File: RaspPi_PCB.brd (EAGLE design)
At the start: 105.4 x 83.8 mm, 5 parts, among them J3 1X2-3.5MM

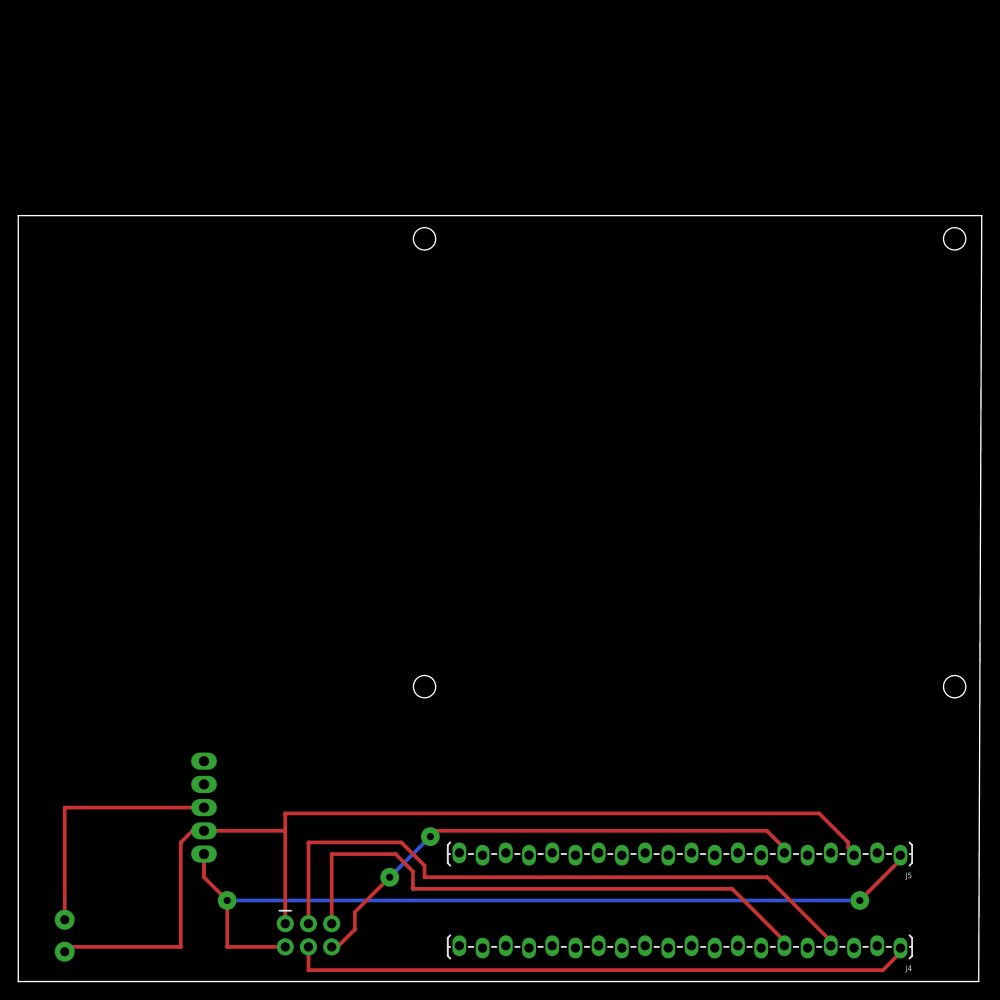
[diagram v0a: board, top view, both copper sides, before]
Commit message: Change RaspPi board to switch the side that the Pi is on and to switch the two Pi headers.
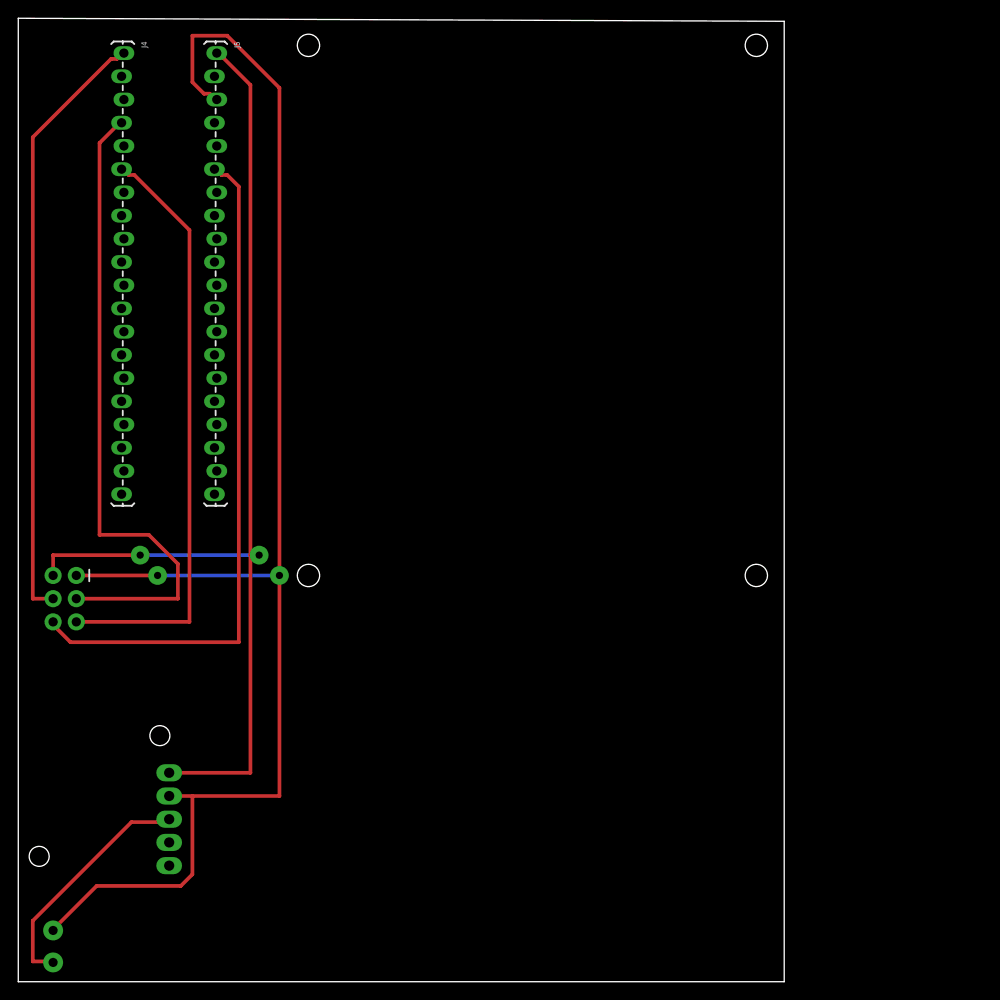
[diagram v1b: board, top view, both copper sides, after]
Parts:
- moved J4 129.6 mm to (11.4, 101.6), turned to 270 degrees
- moved J5 115.3 mm to (21.6, 101.6), turned to 270 degrees
- moved J1 45.5 mm to (5.08, 41.9), turned to 0 degrees
- moved J2 9.67 mm to (16.5, 22.9), turned to 270 degrees
- moved J3 1.80 mm to (3.81, 3.81), turned to 90 degrees
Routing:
- net GND: track 113.3 -> 158.6 mm, vias 0 -> 2
- net 5V: track 93.6 -> 115.0 mm
- net PIN18: track 57.6 -> 74.7 mm, vias 2 -> 0
- net PIN17: track 62.7 -> 65.4 mm
- net 3.3V: track 68.6 -> 66.5 mm
- net VIN: track 27.5 -> 26.3 mm
- net PIN4: track 71.8 -> 71.0 mm
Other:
- board size 105.4 x 83.8 mm -> 83.8 x 105.4 mm

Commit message: Rotate main pcb so it can be printed on the other mill.
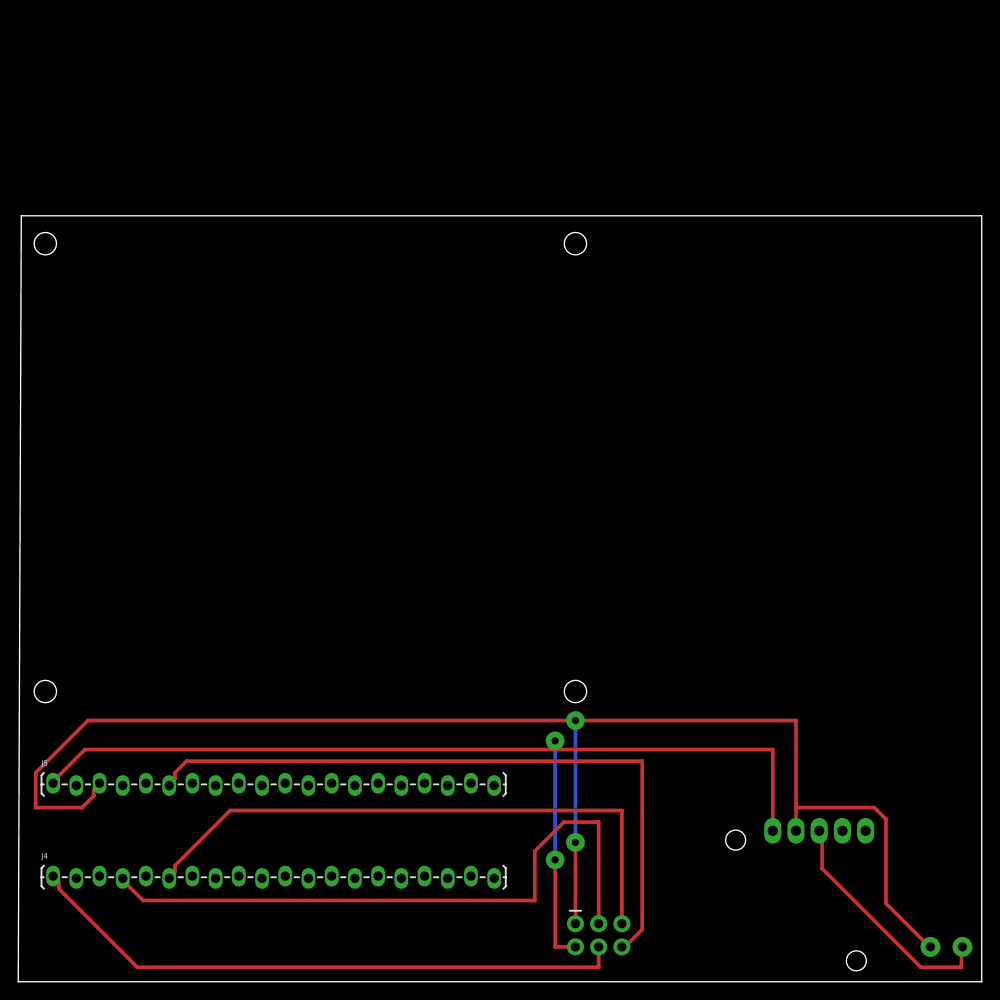
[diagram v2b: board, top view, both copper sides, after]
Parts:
- moved J3 97.8 mm to (101.6, 3.81), turned to 0 degrees
- moved J4 90.5 mm to (3.81, 11.4), turned to 0 degrees
- moved J5 82.0 mm to (3.81, 21.6), turned to 0 degrees
- moved J1 69.1 mm to (63.5, 5.08), turned to 270 degrees
- moved J2 66.3 mm to (82.5, 16.5), turned to 180 degrees
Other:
- board size 83.8 x 105.4 mm -> 105.4 x 83.8 mm

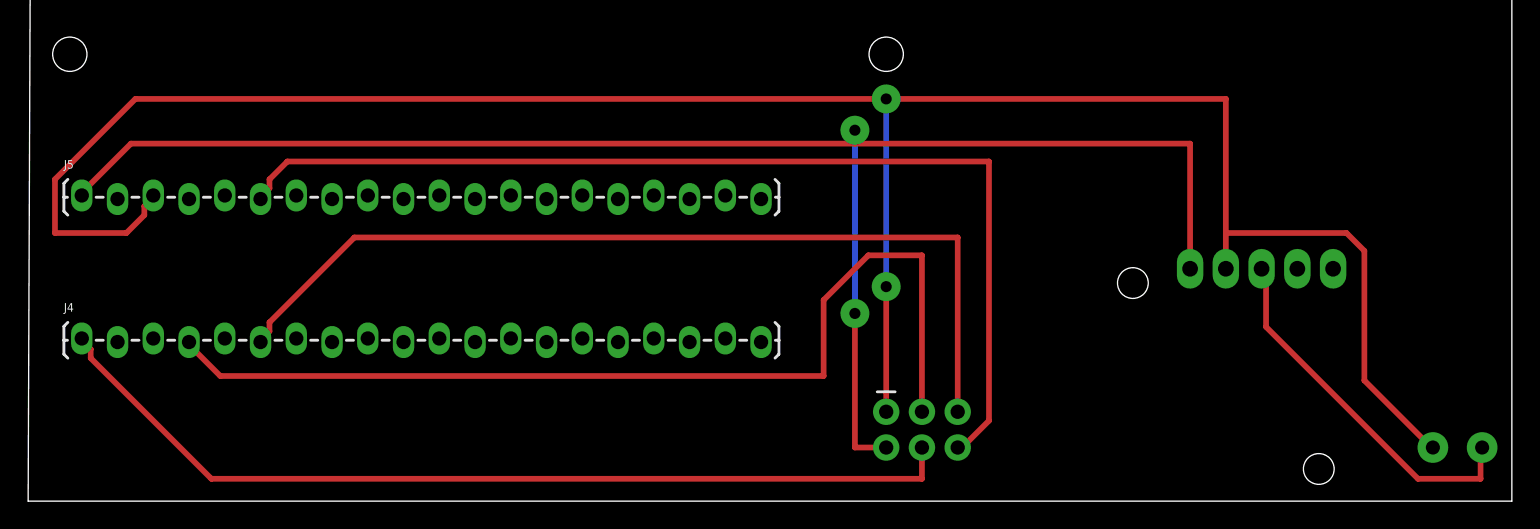
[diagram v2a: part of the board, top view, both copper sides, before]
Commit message: Flip voltage regulator
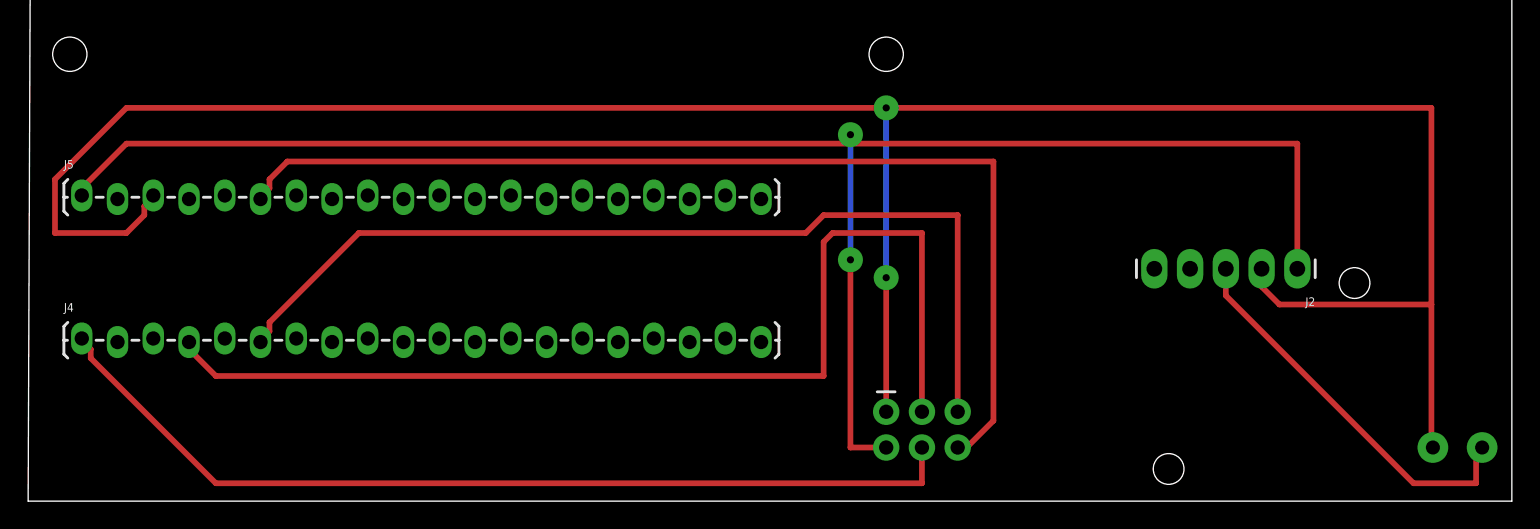
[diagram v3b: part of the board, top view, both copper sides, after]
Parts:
- moved J2 7.62 mm to (90.2, 16.5), flipped to the top
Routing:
- net GND: track 158.6 -> 171.9 mm
- net 5V: track 115.0 -> 122.5 mm
- net PIN4: track 71.0 -> 75.9 mm
- net PIN17: track 65.4 -> 67.7 mm
- net VIN: track 26.3 -> 28.2 mm
- net PIN18: track 74.7 -> 75.4 mm
